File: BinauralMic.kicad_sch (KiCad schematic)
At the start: 0 parts

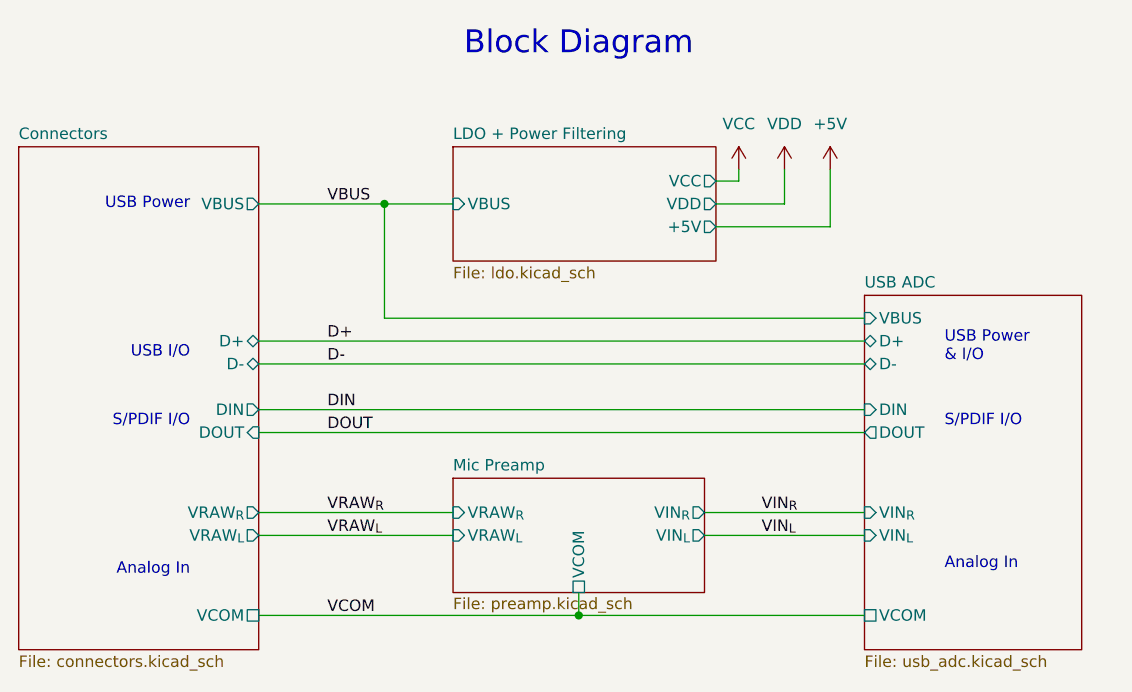
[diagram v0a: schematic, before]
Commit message: Replace S/PIDF RCA jack with a singular one since I won't need an input one
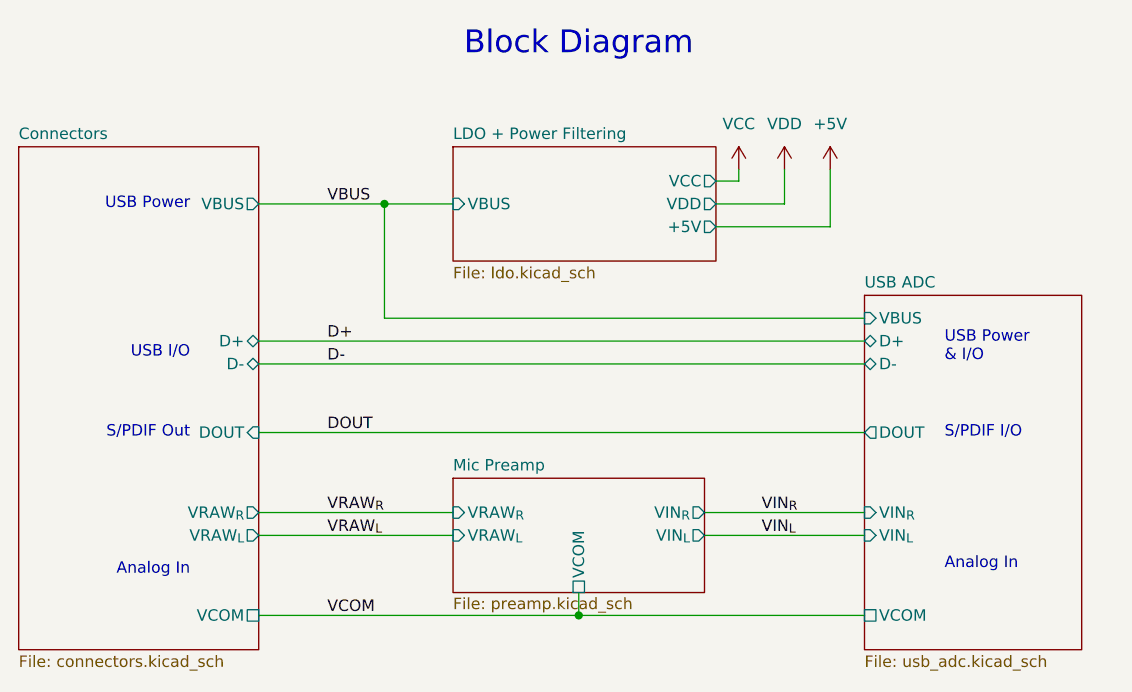
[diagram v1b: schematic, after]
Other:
- sheet Connectors ports: added none; removed DIN
- sheet USB ADC ports: added none; removed DIN
- note added: "S/PDIF Out"
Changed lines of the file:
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@@
-	(wire
-		(pts
-			(xy 68.58 67.31) (xy 135.89 67.31)
-		)
-		(stroke
-			(width 0)
-			(type default)
-		)
-	)
 	(wire
 		(pts
@@
 	(text "S/PDIF I/O"
 		(exclude_from_sim no)
-		(at 144.78 68.58 0)
+		(at 144.78 69.85 0)
 		(effects
 			(font
@@
 		)
 	)
-	(text "S/PDIF I/O"
-		(exclude_from_sim no)
-		(at 60.96 68.58 0)
+	(text "S/PDIF Out"
+		(exclude_from_sim no)
+		(at 60.96 69.85 0)
 		(effects
 			(font
@@
 				(size 2.54 2.54)
 			)
-		)
-	)
-	(label "DIN"
-		(at 76.2 67.31 0)
-		(fields_autoplaced yes)
-		(effects
-			(font
-				(size 1.27 1.27)
-			)
-			(justify left bottom)
 		)
 	)
@@
 			)
 		)
-		(pin "DIN" input
-			(at 135.89 67.31 180)
-			(effects
-				(font
-					(size 1.27 1.27)
-				)
-				(justify left)
-			)
-		)
 		(pin "DOUT" output
 			(at 135.89 69.85 180)
@@
 			(effects
 				(font
-					(size 1.27 1.27)
-				)
-				(justify right)
-			)
-		)
-		(pin "DIN" output
-			(at 68.58 67.31 0)
-			(effects
-				(font

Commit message: More layout, replaced chip crystal with a 2-pin oscillator
All is well with the world
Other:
- sheet LDO + Power Filtering ports: added VCC_{A}; removed VDD
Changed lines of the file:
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@@
+	)
+	(junction
+		(at 121.92 41.91)
+		(diameter 0)
+		(color 0 0 0 0)
 	)
 	(junction
@@
 	(wire
 		(pts
-			(xy 127 44.45) (xy 119.38 44.45)
+			(xy 119.38 44.45) (xy 133.35 44.45)
 		)
 		(stroke
@@
 	(wire
 		(pts
+			(xy 127 41.91) (xy 121.92 41.91)
+		)
+		(stroke
+			(width 0)
+			(type default)
+		)
+	)
+	(wire
+		(pts
 			(xy 68.58 69.85) (xy 135.89 69.85)
 		)
@@
 	(wire
 		(pts
+			(xy 127 40.64) (xy 127 41.91)
+		)
+		(stroke
+			(width 0)
+			(type default)
+		)
+	)
+	(wire
+		(pts
 			(xy 68.58 59.69) (xy 135.89 59.69)
 		)
@@
 	(wire
 		(pts
-			(xy 127 40.64) (xy 127 44.45)
+			(xy 133.35 40.64) (xy 133.35 44.45)
 		)
 		(stroke
@@
 	(wire
 		(pts
-			(xy 132.08 46.99) (xy 119.38 46.99)
+			(xy 139.7 46.99) (xy 119.38 46.99)
 		)
 		(stroke
@@
 	(wire
 		(pts
-			(xy 132.08 40.64) (xy 132.08 46.99)
+			(xy 139.7 40.64) (xy 139.7 46.99)
 		)
 		(stroke
@@
 		(lib_id "power:VDD")
 		(at 127 40.64 0)
+		(mirror y)
 		(unit 1)
 		(exclude_from_sim no)
@@
 		(on_board yes)
 		(dnp no)
-		(fields_autoplaced yes)
 		(property "Reference" "#PWR02"
 			(at 127 44.45 0)
@@
 	)
 	(symbol
-		(lib_id "power:+5V")
-		(at 132.08 40.64 0)
+		(lib_id "power:+3.3VA")
+		(at 133.35 40.64 0)
 		(unit 1)
 		(exclude_from_sim no)
@@
 		(dnp no)
 		(fields_autoplaced yes)
+		(property "Reference" "#PWR031"
+			(at 133.35 44.45 0)
+			(effects
+				(font
+					(size 1.27 1.27)
+				)
+				(hide yes)
+			)
+		)
+		(property "Value" "+3.3VA"
+			(at 133.35 35.56 0)
+			(effects
+				(font
+					(size 1.27 1.27)
+				)
+			)
+		)
+		(property "Footprint" ""
+			(at 133.35 40.64 0)
+			(effects
+				(font
+					(size 1.27 1.27)
+				)
+				(hide yes)
+			)
+		)
+		(property "Datasheet" ""
+			(at 133.35 40.64 0)
+			(effects
+				(font
+					(size 1.27 1.27)
+				)
+				(hide yes)
+			)
+		)
+		(property "Description" "Power symbol creates a global label with name \"+3.3VA\""
+			(at 133.35 40.64 0)
+			(effects
+				(font
+					(size 1.27 1.27)
+				)
+				(hide yes)
+			)
+		)
+		(pin "1"
+		)
+		(instances
+			(project "BinauralMic"
+				(path "/d9e790b9-8aa4-4e58-8bd7-6ef4bc890627"
+					(reference "#PWR031")
+					(unit 1)
+				)
+			)
+		)
+	)
+	(symbol
+		(lib_id "power:+5V")
+		(at 139.7 40.64 0)
+		(unit 1)
+		(exclude_from_sim no)
+		(in_bom yes)
+		(on_board yes)
+		(dnp no)
+		(fields_autoplaced yes)
 		(property "Reference" "#PWR03"
-			(at 132.08 44.45 0)
+			(at 139.7 44.45 0)
 			(effects
 				(font
@@
 		)
 		(property "Value" "+5V"
-			(at 132.08 35.56 0)
+			(at 139.7 35.56 0)
 			(effects
 				(font
@@
 		)
 		(property "Footprint" ""
-			(at 132.08 40.64 0)
+			(at 139.7 40.64 0)
 			(effects
 				(font
@@
 		)
 		(property "Datasheet" ""
-			(at 132.08 40.64 0)
+			(at 139.7 40.64 0)
 			(effects
 				(font
@@
 		)
 		(property "Description" "Power symbol creates a global label with name \"+5V\""
-			(at 132.08 40.64 0)
+			(at 139.7 40.64 0)
 			(effects
 				(font
@@
 			)
 		)
-		(pin "VDD" output
+		(pin "VCC_{A}" output
 			(at 119.38 44.45 0)
 			(effects
